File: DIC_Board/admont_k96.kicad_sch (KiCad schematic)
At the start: 8 parts, among them J30 0430450200, U30 TPS27S100APWPR

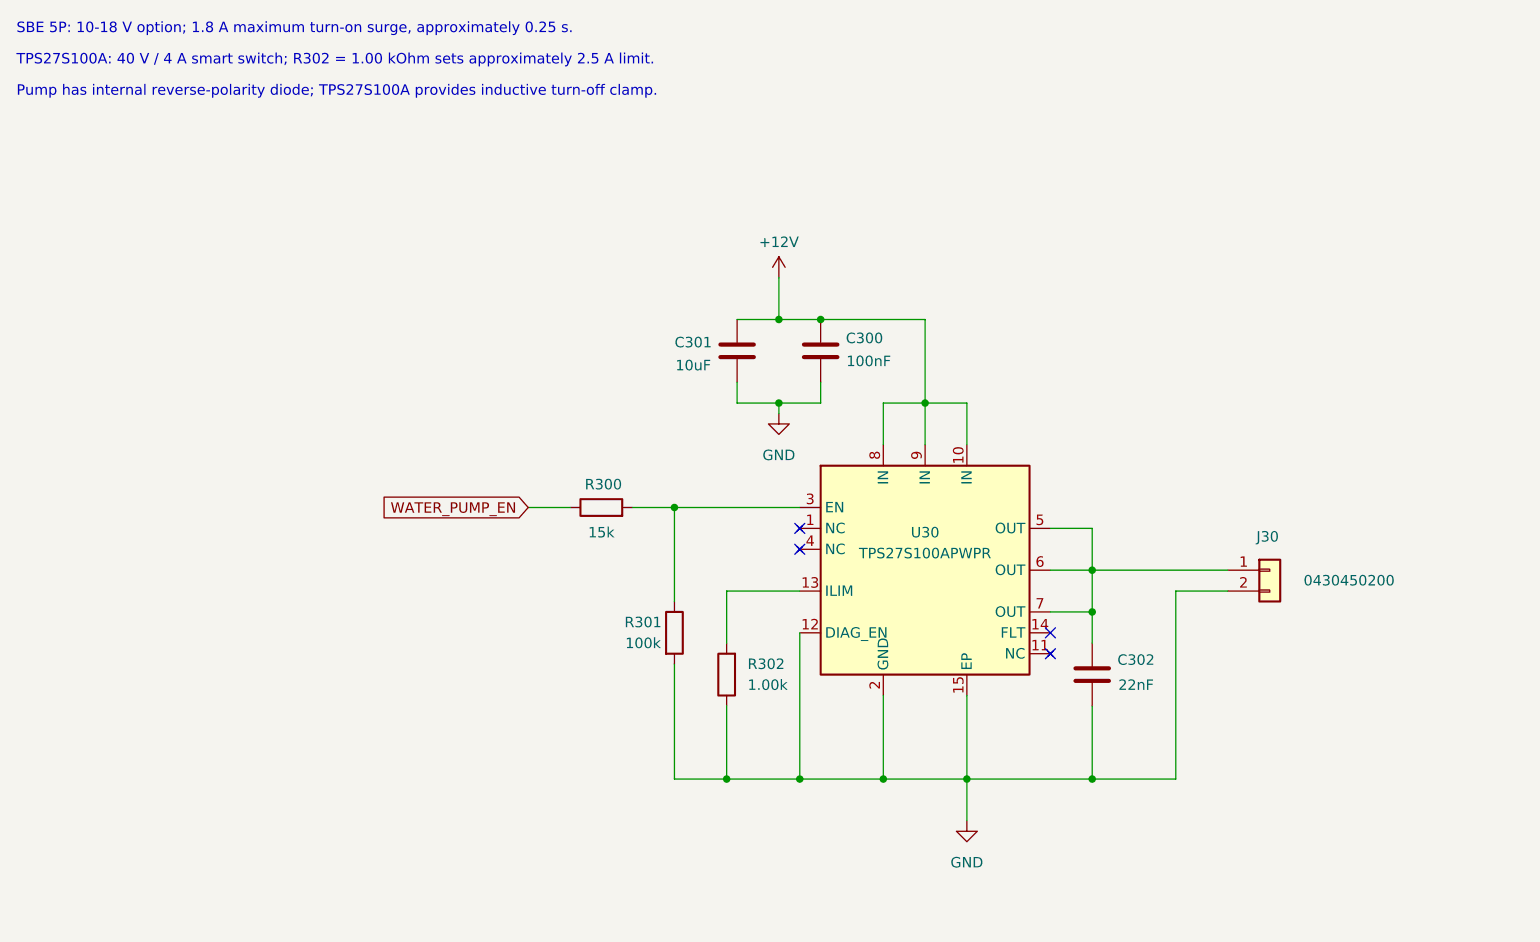
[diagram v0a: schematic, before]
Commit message: Separated the power sheets, did the sensor sheets.
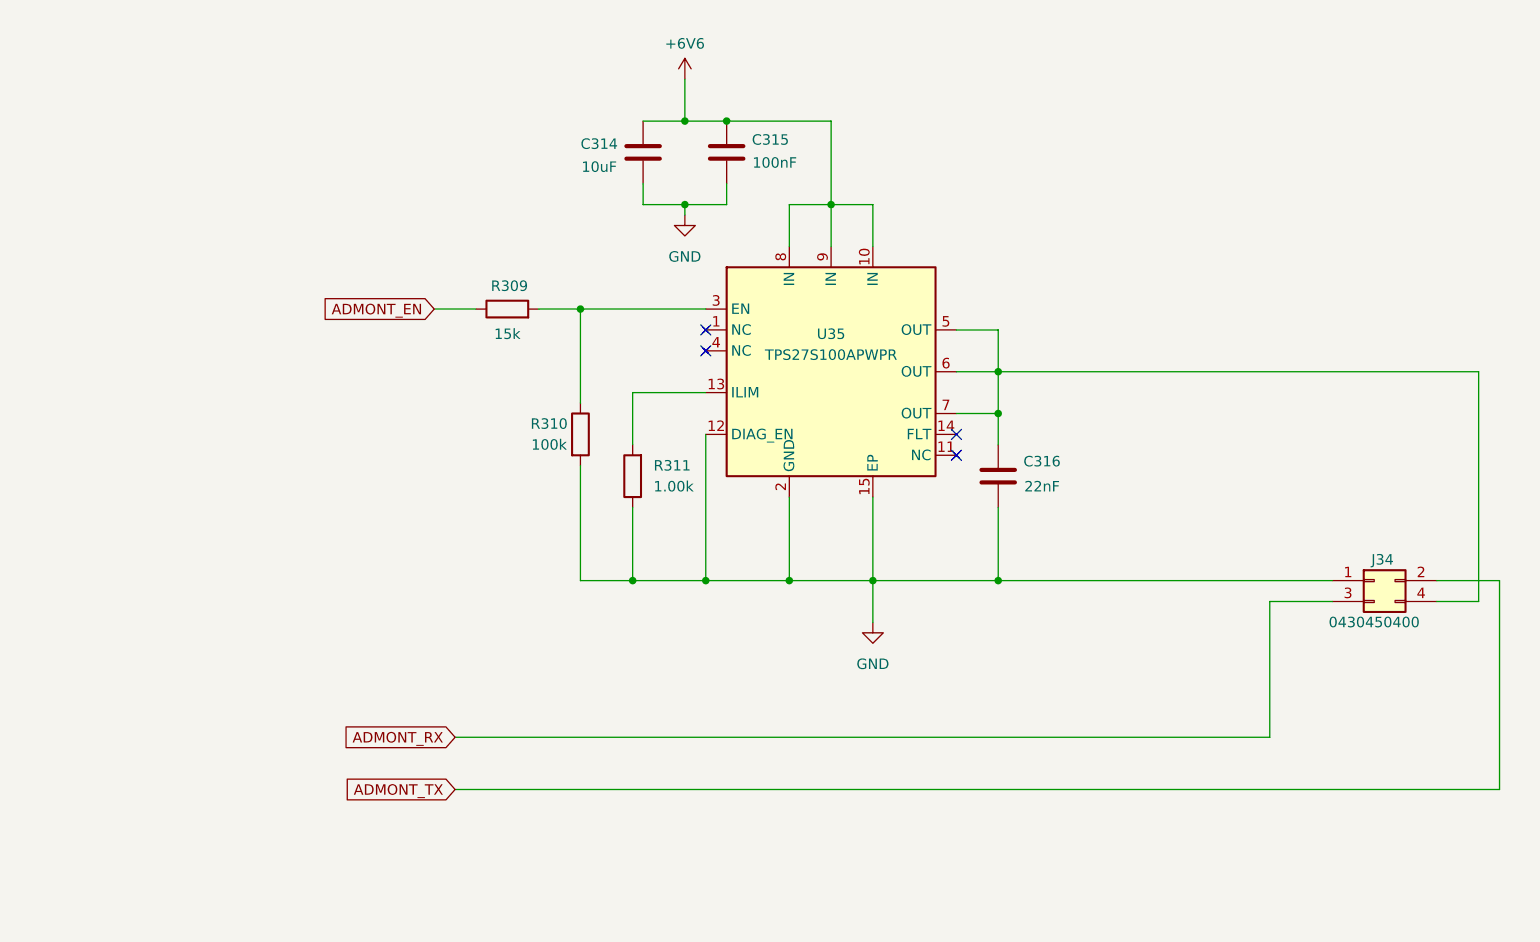
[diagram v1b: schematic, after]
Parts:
- removed C300: 100nF, Capacitor_SMD:C_0402_1005Metric, symbol Device:C
- removed C301: 10uF, Capacitor_SMD:C_1206_3216Metric, symbol Device:C
- removed C302: 22nF, Capacitor_SMD:C_0402_1005Metric, symbol Device:C
- removed J30: 0430450200, Connector_Molex:Molex_Micro-Fit_3.0_43045-0200_2x01_P3.00mm_Horizontal, symbol Connector_Generic:Conn_01x02
- removed R300: 15k, Resistor_SMD:R_0402_1005Metric, symbol Device:R
- removed R301: 100k, Resistor_SMD:R_0402_1005Metric, symbol Device:R
- removed R302: 1.00k, Resistor_SMD:R_0402_1005Metric, symbol Device:R
- removed U30: TPS27S100APWPR, Package_SO:Texas_HTSSOP-14-1EP_4.4x5mm_P0.65mm_EP3.4x5mm_Mask3.155x3.255mm_ThermalVias, symbol DIC_Board:TPS27S100A
- added C314: 10uF, Capacitor_SMD:C_1206_3216Metric, symbol Device:C
- added C315: 100nF, Capacitor_SMD:C_0402_1005Metric, symbol Device:C
- added C316: 22nF, Capacitor_SMD:C_0402_1005Metric, symbol Device:C
- added J34: 0430450400, Connector_Molex:Molex_Micro-Fit_3.0_43045-0400_2x02_P3.00mm_Horizontal, symbol Connector_Generic:Conn_02x02_Odd_Even
- added R309: 15k, Resistor_SMD:R_0402_1005Metric, symbol Device:R
- added R310: 100k, Resistor_SMD:R_0402_1005Metric, symbol Device:R
- added R311: 1.00k, Resistor_SMD:R_0402_1005Metric, symbol Device:R
- added U35: TPS27S100APWPR, Package_SO:Texas_HTSSOP-14-1EP_4.4x5mm_P0.65mm_EP3.4x5mm_Mask3.155x3.255mm_ThermalVias, symbol DIC_Board:TPS27S100A
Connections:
- net GND: now also C314.2, C315.2, C316.2, J34.1 (Pin_1), R310.2, R311.1, U35.12 (DIAG_EN), U35.15 (EP), U35.2 (GND)
- new net: C316.1, J34.4 (Pin_4), U35.5 (OUT), U35.6 (OUT), U35.7 (OUT)
- new net: R309.2, R310.1, U35.3 (EN)
- new net: R311.2, U35.13 (ILIM)
- new net +6V6: C314.1, C315.1, U35.10 (IN), U35.8 (IN), U35.9 (IN)
- new net ADMONT_EN: R309.1
- new net ADMONT_RX: J34.3 (Pin_3)
- new net ADMONT_TX: J34.2 (Pin_2)
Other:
- note removed: "Pump has internal reverse-polarity diode; TPS27S100A provides inductive turn-off clamp."
- note removed: "SBE 5P: 10-18 V option; 1.8 A maximum turn-on surge, approximately 0.25 s."
- note removed: "TPS27S100A: 40 V / 4 A smart switch; R302 = 1.00 kOhm sets approximately 2.5 A limit."
- title: Water Pump -> (none)

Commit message: Wrapping up schematic
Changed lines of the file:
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@@
 	)
 	(global_label "ADMONT_RX"
-		(shape input)
+		(shape output)
 		(at 82.55 109.22 180)
 		(fields_autoplaced yes)

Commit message: Checkpoint current schematic state
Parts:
- removed J34: 0430450400, Connector_Molex:Molex_Micro-Fit_3.0_43045-0400_2x02_P3.00mm_Horizontal, symbol Connector_Generic:Conn_02x02_Odd_Even
- added J8: Conn_01x04, symbol Connector_Generic:Conn_01x04
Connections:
- net ADMONT_RX: now also J8.3 (Pin_3)
- net ADMONT_TX: now also J8.2 (Pin_2)
- net GND: now also J8.1 (Pin_1)
- net at C316.1, U35.5 (OUT), U35.6 (OUT)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: now also J8.4 (Pin_4)
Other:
- moved on the sheet: C314, C315, C316, R309, R310, R311, U35

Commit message: Synchronize schematic hierarchy and MCU pin map
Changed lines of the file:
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@@
 		)
 	)
-	(global_label "ADMONT_TX"
+	(hierarchical_label "ADMONT_TX"
 		(shape input)
 		(at 186.69 104.14 180)
-		(fields_autoplaced yes)
 		(effects
 			(font
@@
 			(justify right)
 		)
-		(property "Intersheetrefs" "${INTERSHEET_REFS}"
-			(at 173.1215 104.14 0)
-			(hide yes)
-			(show_name no)
-			(do_not_autoplace no)
-			(effects
-				(font
-					(size 1.27 1.27)
-				)
-				(justify right)
-			)
-		)
 	)
-	(global_label "ADMONT_RX"
+	(hierarchical_label "ADMONT_RX"
 		(shape output)
 		(at 186.69 106.68 180)
-		(fields_autoplaced yes)
 		(effects
 			(font
@@
 			(justify right)
 		)
-		(property "Intersheetrefs" "${INTERSHEET_REFS}"
-			(at 172.8191 106.68 0)
-			(hide yes)
-			(show_name no)
-			(do_not_autoplace no)
-			(effects
-				(font
-					(size 1.27 1.27)
-				)
-				(justify right)
-			)
-		)
 	)
-	(global_label "ADMONT_EN"
+	(hierarchical_label "ADMONT_EN"
 		(shape input)
 		(at 68.58 87.63 180)
-		(fields_autoplaced yes)
 		(effects
 			(font
@@
 			(justify right)
 		)
-		(property "Intersheetrefs" "${INTERSHEET_REFS}"
-			(at 54.7091 87.63 0)
-			(hide yes)
-			(show_name no)
-			(do_not_autoplace no)
-			(effects
-				(font
-					(size 1.27 1.27)
-				)
-				(justify right)
-			)
-		)
 	)

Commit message: Updated board for layout! All footprints added
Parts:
- J8: footprint (none) -> Connector_Molex:Molex_Micro-Fit_3.0_43045-0400_2x02_P3.00mm_Horizontal; BOM Source (none) -> https://www.molex.com/en-us/products/part-detail/430450400; Design Confirmation (none) -> 2026-09-11: User confirmed the existing K96 interface and s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; MPN (none) -> 0430450400; Manufacturer (none) -> Molex
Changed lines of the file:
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@@
 	)
 	(symbol
-		(lib_id "power:+6V6")
+		(lib_id "DIC_Board:+6V6")
 		(at 99.06 59.69 0)
 		(unit 1)
@@
 			)
 		)
-		(property "Footprint" ""
+		(property "Footprint" "Connector_Molex:Molex_Micro-Fit_3.0_43045-0400_2x02_P3.00mm_Horizontal"
 			(at 196.85 104.14 0)
 			(hide yes)
@@
 			(hide yes)
 			(show_name no)
+			(do_not_autoplace no)
+			(effects
+				(font
+					(size 1.27 1.27)
+				)
+			)
+		)
+		(property "Design Confirmation" "2026-09-11: User confirmed the existing K96 interface and supply are acceptable; retain the implemented interface."
+			(at 0 0 0)
+			(hide yes)
+			(show_name no)
+			(do_not_autoplace no)
+			(effects
+				(font
+					(size 1.27 1.27)
+				)
+			)
+		)
+		(property "MPN" "0430450400"
+			(at 0 0 0)
+			(hide yes)
+			(show_name no)
+			(do_not_autoplace no)
+			(effects
+				(font
+					(size 1.27 1.27)
+				)
+			)
+		)
+		(property "Manufacturer" "Molex"
+			(at 0 0 0)
+			(hide yes)
+			(show_name no)
+			(do_not_autoplace no)
+			(effects
+				(font
+					(size 1.27 1.27)
+				)
+			)
+		)
+		(property "BOM Source" "https://www.molex.com/en-us/products/part-detail/430450400"
+			(at 0 0 0)
+			(hide yes)
+			(show_name no)

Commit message: Let gpt6 astra have a go at routing. bad results.
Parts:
- U35: footprint Package_SO:Texas_HTSSOP-14-1EP_4.4x5mm_P0.65mm_EP3.4x5mm_Mask3.155x3.255mm_ThermalVias -> DIC_Board:TPS27S100_Thermal_Drill0p3
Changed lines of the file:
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@@
 			)
 		)
-		(property "Footprint" "Package_SO:Texas_HTSSOP-14-1EP_4.4x5mm_P0.65mm_EP3.4x5mm_Mask3.155x3.255mm_ThermalVias"
+		(property "Footprint" "DIC_Board:TPS27S100_Thermal_Drill0p3"
 			(at 116.84 95.25 0)
 			(hide yes)
